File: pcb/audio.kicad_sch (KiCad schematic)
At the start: 20 parts, among them J9 Conn_01x03, U17 PCM5102A

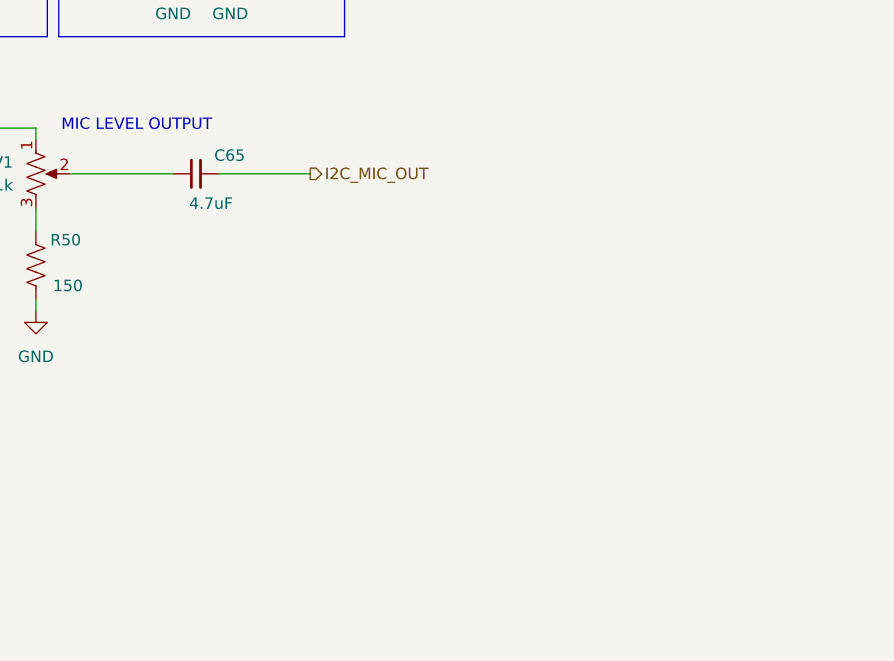
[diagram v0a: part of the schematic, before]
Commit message: Add external HT jack (J11) and PTT keying FET (Q10)
J11 (CUI/Same Sky SJ2-3593D-SMT-TR, switched TRS): tip and ring
switches auto-disconnect the onboard SA818S audio/PTT feeds the
instant something is plugged in. Q10 (BSS138) keys the shared PTT
node from GPIO16, with R53 (10k) pull-up holding it released by
default. Reviewed: T/TN and R/RN wiring both verified correct
against the jack's normalling behavior.

Co-Authored-By: Claude Sonnet 5 <noreply@anthropic.com>
Claude-Session: https://claude.ai/code/session_01LhLkuH6sQ5GbUZ61bG7p2h
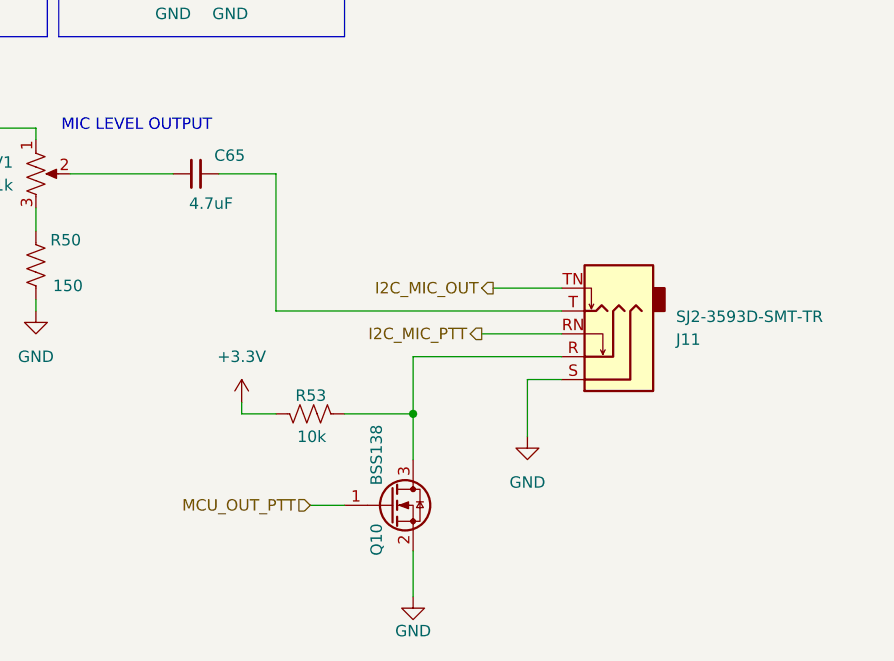
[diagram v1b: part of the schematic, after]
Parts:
- added J11: SJ2-3593D-SMT-TR, Connector_Audio:Jack_3.5mm_CUI_SJ2-3593D-SMT_Horizontal, symbol Connector_Audio:AudioJack3_SwitchTR
- added Q10: BSS138, Package_TO_SOT_SMD:SOT-23, symbol Transistor_FET:BSS138
- added R53: 10k, Resistor_SMD:R_0603_1608Metric, symbol Device:R_US
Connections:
- net +3.3V: now also R53.2
- net GND: now also J11.S, Q10.2 (S)
- net I2C_MIC_OUT: now also J11.TN; no longer C65.1
- new net: J11.R, Q10.3 (D), R53.1
- new net: C65.1, J11.T
- new net I2C_MIC_PTT: J11.RN
- new net MCU_OUT_PTT: Q10.1 (G)

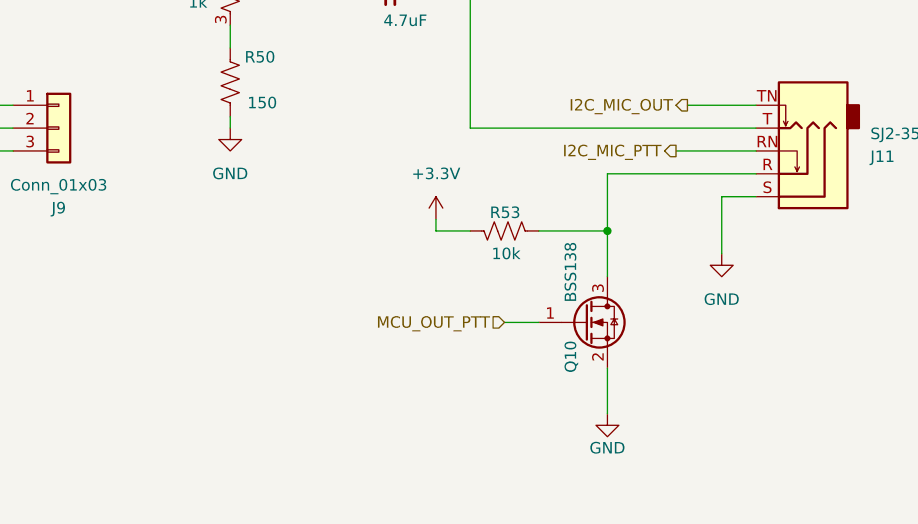
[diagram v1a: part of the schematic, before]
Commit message: Wire SA818 PD/H-L and PTT opto, GPS power gating with bench bypass, RF detector groundwork
- SA818S-V: wire PD/H-L to PCA9555 expander outputs; swap PTT-keying FET
  for PC817 optocoupler isolation on the shared SA818S/external-HT PTT line
- GPS: add Q10 (AO3407A) high-side P-FET gating VCC+VCC_IO together for
  genuine hardware backup mode, driven via Q13 level-shifter from a new
  PCA9555 output (PERIPH_OUT_GPS_PWRON); add JP28 as a source-to-drain
  bench bypass across Q10 for unconditional power during bring-up; wire
  EXTINT to another PCA9555 output (PERIPH_OUT_GPS_EXTINT, pulled low by
  R57) to experiment with UART software-standby + external wake
- peripherals: reassign PCA9555 channels for the above plus SA818 PD/H-L
- audio/mcu-esp32: forward-power detector tap wiring groundwork
- docs: add vhf_matching_detector.md (matching network + RF detector BOM
  and layout), index it in _docs/README.md

Co-Authored-By: Claude Sonnet 5 <noreply@anthropic.com>
Claude-Session: https://claude.ai/code/session_01LhLkuH6sQ5GbUZ61bG7p2h
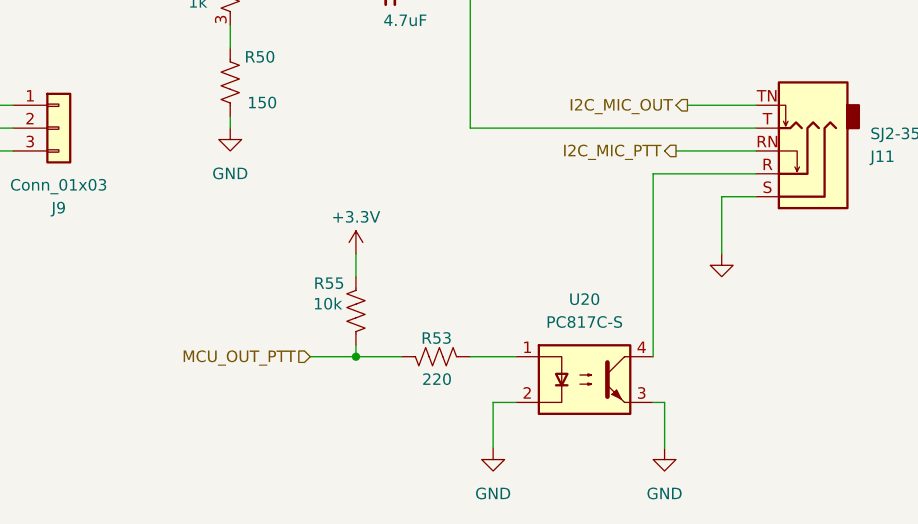
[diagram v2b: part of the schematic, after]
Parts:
- removed Q10: BSS138, Package_TO_SOT_SMD:SOT-23, symbol Transistor_FET:BSS138
- added R55: 10k, Resistor_SMD:R_0603_1608Metric, symbol Device:R_US
- added U20: PC817C-S, Package_SO:SOP-4_7.5x4.1mm_P2.54mm, symbol Isolator:PC817
- R53: value 10k -> 220; LCSC Part # C95204 -> C107696; MPN RT0603BRD0710KL -> RC0603FR-07220RL
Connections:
- net +3.3V: now also R55.2; no longer R53.2
- net GND: now also U20.2, U20.3
- net MCU_OUT_PTT: now also R53.2, R55.1
- net at R53.1: now also U20.1; no longer J11.R
- new net: J11.R, U20.4
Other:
- moved on the sheet: R53
